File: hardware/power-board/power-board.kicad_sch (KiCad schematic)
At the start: 25 parts, among them J1 SW_SPST, J2 Conn_01x04, J3 DMX512 Out Jack, J4 DMX512, K1 SPST-NO, K2 SPST-NO, P1 IEC320-C14, P2 IEC320-C13, P3 IEC320-C13, U1 NUD3112DMT1G, U2 MAX3075E

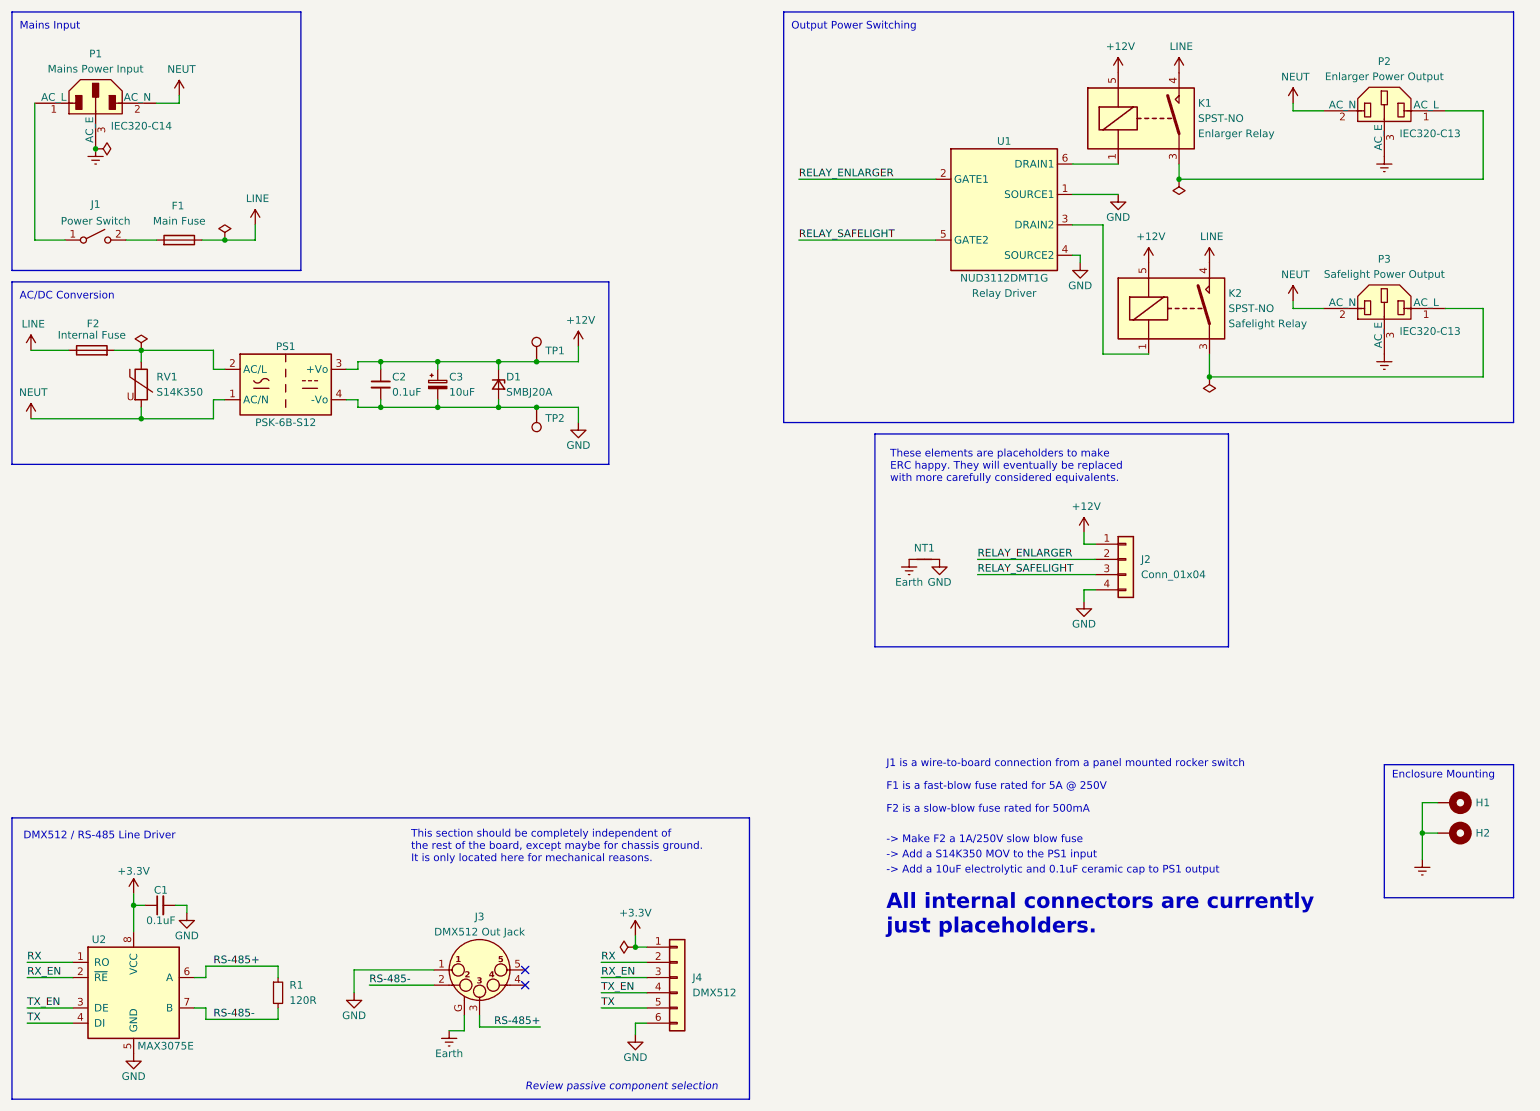
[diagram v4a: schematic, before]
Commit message: Schematic updates and component assignment
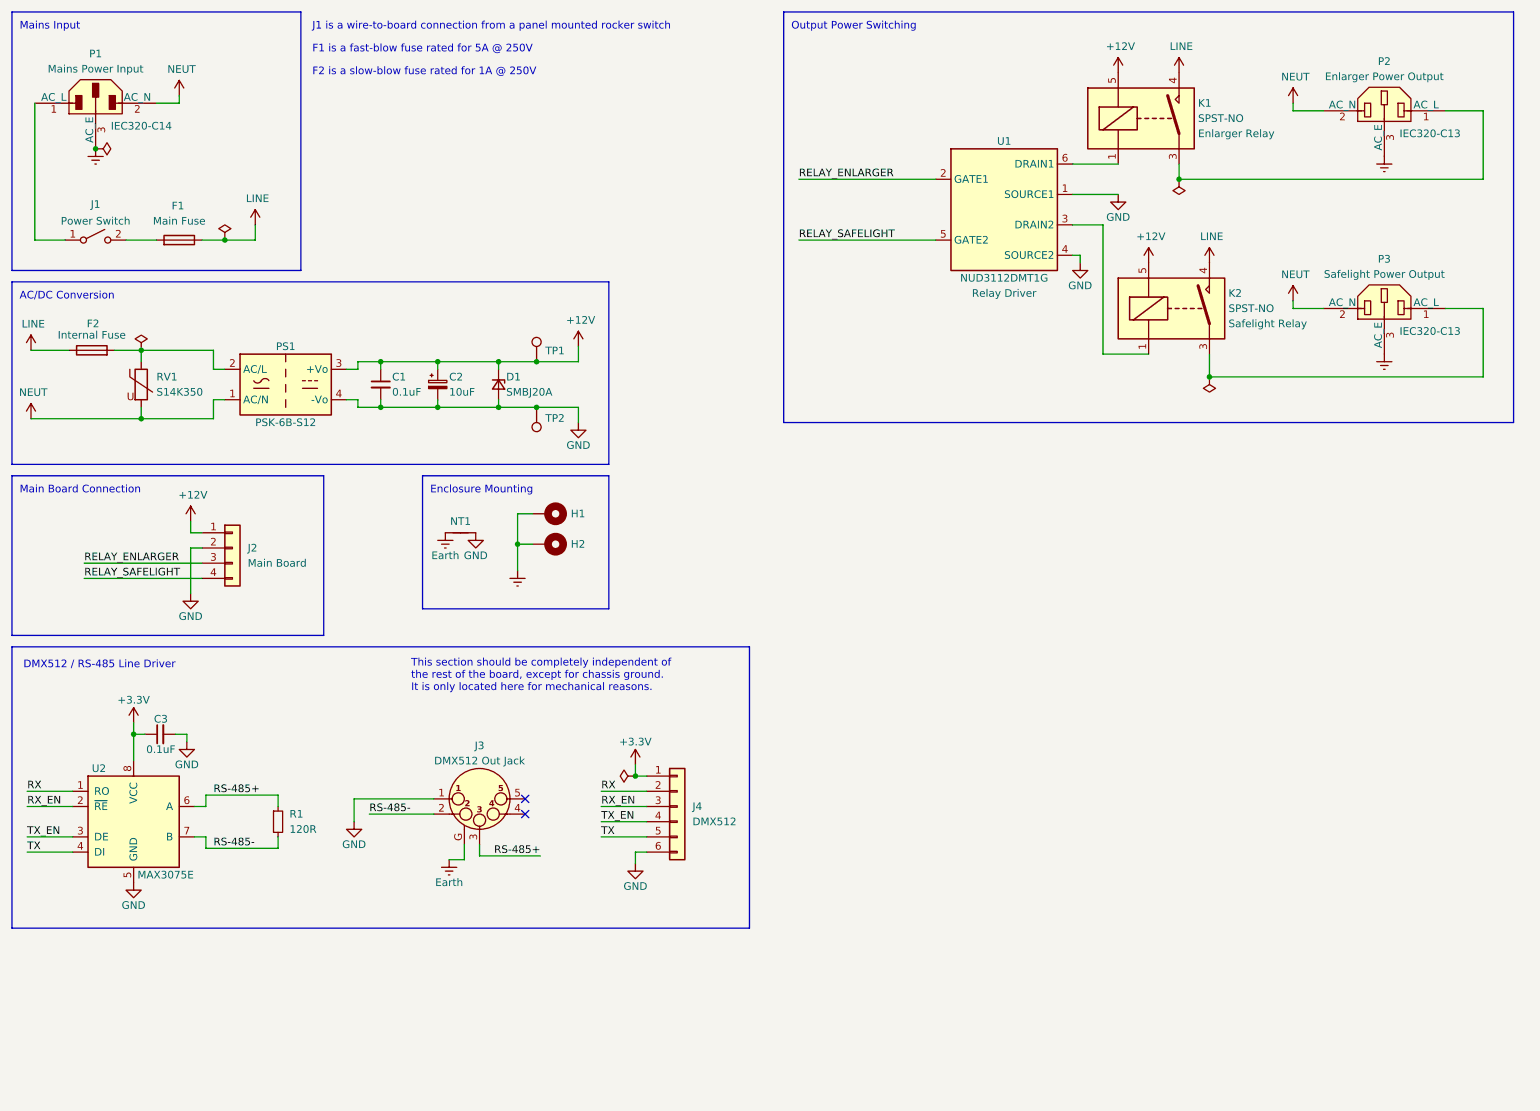
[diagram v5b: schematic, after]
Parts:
- C3: renamed from C1; Manufacturer (none) -> Samsung Electro-Mechanics; Manufacturer PN (none) -> CL21B104KBFNNNE; Supplier (none) -> Digi-Key; Supplier PN (none) -> 1276-1180-1-ND
- J2: value Conn_01x04 -> Main Board; footprint Connector_JST:JST_EH_B4B-EH-A_1x04_P2.50mm_Vertical -> Connector_JST:JST_PH_S4B-PH-SM4-TB_1x04-1MP_P2.00mm_Horizontal; Manufacturer (none) -> JST Sales America Inc.; Manufacturer PN (none) -> S4B-PH-SM4-TB(LF)(SN); Supplier (none) -> Digi-Key; Supplier PN (none) -> 455-1751-1-ND
- J4: footprint Connector_JST:JST_EH_B6B-EH-A_1x06_P2.50mm_Vertical -> Connector_JST:JST_SH_SM06B-SRSS-TB_1x06-1MP_P1.00mm_Horizontal; Manufacturer (none) -> JST Sales America Inc.; Manufacturer PN (none) -> SM06B-SRSS-TB(LF)(SN); Supplier (none) -> Digi-Key; Supplier PN (none) -> 455-1806-1-ND
- R1: Manufacturer (none) -> Vishay Dale; Manufacturer PN (none) -> CRCW0805120RFKEA; Supplier (none) -> Digi-Key; Supplier PN (none) -> 541-120CCT-ND
- renumbered C2 to C1, C3 to C2
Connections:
- net GND: now also J2.2 (Pin_2); no longer J2.4 (Pin_4)
- net RELAY_ENLARGER: now also J2.3 (Pin_3); no longer J2.2 (Pin_2)
- net RELAY_SAFELIGHT: now also J2.4 (Pin_4); no longer J2.3 (Pin_3)
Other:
- note added: "F2 is a slow-blow fuse rated for 1A @ 250V"
- note added: "Main Board Connection"
- note added: "This section should be completely independent of the rest of the board, except for chassis ground. It is only located here for mechanical reasons."
- note removed: "-> Add a 10uF electrolytic and 0.1uF ceramic cap to PS1 output"
- note removed: "-> Add a S14K350 MOV to the PS1 input"
- note removed: "-> Make F2 a 1A/250V slow blow fuse"
- note removed: "All internal connectors are currently just placeholders."
- note removed: "F2 is a slow-blow fuse rated for 500mA"
- note removed: "Review passive component selection"
- note removed: "These elements are placeholders to make ERC happy. They will eventually be replaced with more carefully considered equivalents."
- note removed: "This section should be completely independent of the rest of the board, except maybe for chassis ground. It is only located here for mechanical reasons."
- moved on the sheet: C3, H1, H2, J2, J3, J4, NT1, R1, U2

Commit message: Updated PCB layout, still refining things
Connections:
- net GND: no longer C3.2, J3.1 (P1), J4.6 (Pin_6), U2.5 (GND)
- new net GND1: C3.2, J3.1 (P1), J4.6 (Pin_6), U2.5 (GND)
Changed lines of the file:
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@@
   (junction (at 95.25 80.01) (diameter 0) (color 0 0 0 0)
+  )
+  (junction (at 118.11 154.305) (diameter 0) (color 0 0 0 0)
   )
   (junction (at 49.53 52.07) (diameter 0) (color 0 0 0 0)
@@
     (pin "2")
   )
-  (symbol (lib_id "power:GND") (at 43.18 135.89 0) (unit 1)
-    (in_bom yes) (on_board yes)
-    (property "Reference" "#PWR023" (id 0) (at 43.18 142.24 0)
-      (effects (font (size 1.27 1.27)) hide)
-    )
-    (property "Value" "GND" (id 1) (at 43.18 139.7 0))
-    (property "Footprint" "" (id 2) (at 43.18 135.89 0)
-      (effects (font (size 1.27 1.27)) hide)
-    )
-    (property "Datasheet" "" (id 3) (at 43.18 135.89 0)
-      (effects (font (size 1.27 1.27)) hide)
-    )
-    (pin "1")
-  )
   (symbol (lib_id "Project:Conn_PX0580-PC") (at 27.94 29.21 0) (unit 1)
     (in_bom yes) (on_board yes)
@@
     (pin "2")
     (pin "3")
+  )
+  (symbol (lib_id "power:GND1") (at 118.11 156.21 0) (unit 1)
+    (in_bom yes) (on_board yes)
+    (property "Reference" "#PWR028" (id 0) (at 118.11 162.56 0)
+      (effects (font (size 1.27 1.27)) hide)
+    )
+    (property "Value" "GND1" (id 1) (at 118.11 160.02 0))
+    (property "Footprint" "" (id 2) (at 118.11 156.21 0)
+      (effects (font (size 1.27 1.27)) hide)
+    )
+    (property "Datasheet" "" (id 3) (at 118.11 156.21 0)
+      (effects (font (size 1.27 1.27)) hide)
+    )
+    (pin "1")
+  )
+  (symbol (lib_id "power:GND1") (at 43.18 135.89 0) (unit 1)
+    (in_bom yes) (on_board yes)
+    (property "Reference" "#PWR023" (id 0) (at 43.18 142.24 0)
+      (effects (font (size 1.27 1.27)) hide)
+    )
+    (property "Value" "GND1" (id 1) (at 43.18 139.7 0))
+    (property "Footprint" "" (id 2) (at 43.18 135.89 0)
+      (effects (font (size 1.27 1.27)) hide)
+    )
+    (property "Datasheet" "" (id 3) (at 43.18 135.89 0)
+      (effects (font (size 1.27 1.27)) hide)
+    )
+    (pin "1")
   )
   (symbol (lib_id "Device:NetTie_2") (at 88.9 100.965 0) (unit 1)
@@
     (pin "1")
     (pin "2")
+  )
+  (symbol (lib_id "power:GND1") (at 34.29 159.385 0) (unit 1)
+    (in_bom yes) (on_board yes)
+    (property "Reference" "#PWR022" (id 0) (at 34.29 165.735 0)
+      (effects (font (size 1.27 1.27)) hide)
+    )
+    (property "Value" "GND1" (id 1) (at 34.29 163.195 0))
+    (property "Footprint" "" (id 2) (at 34.29 159.385 0)
+      (effects (font (size 1.27 1.27)) hide)
+    )
+    (property "Datasheet" "" (id 3) (at 34.29 159.385 0)
+      (effects (font (size 1.27 1.27)) hide)
+    )
+    (pin "1")
   )
   (symbol (lib_id "power:+12V") (at 198.755 24.13 0) (unit 1)
@@
     (pin "1")
   )
-  (symbol (lib_id "power:GND") (at 118.11 156.21 0) (unit 1)
-    (in_bom yes) (on_board yes)
-    (property "Reference" "#PWR028" (id 0) (at 118.11 162.56 0)
-      (effects (font (size 1.27 1.27)) hide)
-    )
-    (property "Value" "GND" (id 1) (at 118.11 160.02 0))
-    (property "Footprint" "" (id 2) (at 118.11 156.21 0)
-      (effects (font (size 1.27 1.27)) hide)
-    )
-    (property "Datasheet" "" (id 3) (at 118.11 156.21 0)
-      (effects (font (size 1.27 1.27)) hide)
-    )
-    (pin "1")
-  )
   (symbol (lib_id "Device:C_Small") (at 38.735 134.62 90) (unit 1)
     (in_bom yes) (on_board yes)
@@
     )
     (property "Datasheet" "~" (id 3) (at 243.205 71.12 0)
+      (effects (font (size 1.27 1.27)) hide)
+    )
+    (pin "1")
+  )
+  (symbol (lib_id "power:PWR_FLAG") (at 118.11 154.305 90) (unit 1)
+    (in_bom yes) (on_board yes)
+    (property "Reference" "#FLG07" (id 0) (at 116.205 154.305 0)
+      (effects (font (size 1.27 1.27)) hide)
+    )
+    (property "Value" "PWR_FLAG" (id 1) (at 114.3 154.305 0)
+      (effects (font (size 1.27 1.27)) hide)
+    )
+    (property "Footprint" "" (id 2) (at 118.11 154.305 0)
+      (effects (font (size 1.27 1.27)) hide)
+    )
+    (property "Datasheet" "~" (id 3) (at 118.11 154.305 0)
       (effects (font (size 1.27 1.27)) hide)
     )
@@
     (pin "1")
   )
-  (symbol (lib_id "power:GND") (at 71.12 149.225 0) (unit 1)
-    (in_bom yes) (on_board yes)
-    (property "Reference" "#PWR024" (id 0) (at 71.12 155.575 0)
-      (effects (font (size 1.27 1.27)) hide)
-    )
-    (property "Value" "GND" (id 1) (at 71.12 153.035 0))
-    (property "Footprint" "" (id 2) (at 71.12 149.225 0)
-      (effects (font (size 1.27 1.27)) hide)
-    )
-    (property "Datasheet" "" (id 3) (at 71.12 149.225 0)
-      (effects (font (size 1.27 1.27)) hide)
-    )
-    (pin "1")
-  )
   (symbol (lib_id "power:PWR_FLAG") (at 27.94 36.83 270) (unit 1)
     (in_bom yes) (on_board yes)
@@
     (pin "1")
   )
-  (symbol (lib_id "power:GND") (at 34.29 159.385 0) (unit 1)
-    (in_bom yes) (on_board yes)
-    (property "Reference" "#PWR022" (id 0) (at 34.29 165.735 0)
-      (effects (font (size 1.27 1.27)) hide)
-    )
-    (property "Value" "GND" (id 1) (at 34.29 163.195 0))
-    (property "Footprint" "" (id 2) (at 34.29 159.385 0)
-      (effects (font (size 1.27 1.27)) hide)
-    )
-    (property "Datasheet" "" (id 3) (at 34.29 159.385 0)
-      (effects (font (size 1.27 1.27)) hide)
-    )
-    (pin "1")
-  )
   (symbol (lib_id "Project:PSK-6B-S12") (at 59.69 76.2 0) (unit 1)
     (in_bom yes) (on_board yes)
@@
     )
     (property "Datasheet" "" (id 3) (at 208.915 24.13 0)
+      (effects (font (size 1.27 1.27)) hide)
+    )
+    (pin "1")
+  )
+  (symbol (lib_id "power:GND1") (at 71.12 149.225 0) (unit 1)
+    (in_bom yes) (on_board yes)
+    (property "Reference" "#PWR024" (id 0) (at 71.12 155.575 0)
+      (effects (font (size 1.27 1.27)) hide)
+    )
+    (property "Value" "GND1" (id 1) (at 71.12 153.035 0))
+    (property "Footprint" "" (id 2) (at 71.12 149.225 0)
+      (effects (font (size 1.27 1.27)) hide)
+    )
+    (property "Datasheet" "" (id 3) (at 71.12 149.225 0)
       (effects (font (size 1.27 1.27)) hide)
     )
@@
       (reference "#FLG06") (unit 1) (value "PWR_FLAG") (footprint "")
     )
+    (path "/ad7505eb-addd-47cc-b830-1245109c476f"
+      (reference "#FLG07") (unit 1) (value "PWR_FLAG") (footprint "")
+    )
     (path "/f3f865b6-c7a0-4dde-9cf7-4763a1295ea1"
       (reference "#PWR01") (unit 1) (value "Earth") (footprint "")
@@
       (reference "#PWR021") (unit 1) (value "GND") (footprint "")
     )
-    (path "/f414fade-2297-4152-a754-c86f8c9e7f90"
-      (reference "#PWR022") (unit 1) (value "GND") (footprint "")
-    )
-    (path "/203ef615-4332-432b-b07c-2f82589530ea"
-      (reference "#PWR023") (unit 1) (value "GND") (footprint "")
-    )
-    (path "/e8afdcb2-93ca-4bac-b467-43551ac02a9b"
-      (reference "#PWR024") (unit 1) (value "GND") (footprint "")
+    (path "/53d9ccd4-509a-405c-b060-9272127d6e5b"
+      (reference "#PWR022") (unit 1) (value "GND1") (footprint "")
+    )
+    (path "/3b543809-26ac-49f8-a798-fec846360a65"
+      (reference "#PWR023") (unit 1) (value "GND1") (footprint "")
+    )
+    (path "/f6ff6ac4-3ace-4502-84b0-e74ef7bc8c30"
+      (reference "#PWR024") (unit 1) (value "GND1") (footprint "")
     )
     (path "/09bf7df5-a2b0-47eb-a4b1-0b40fec050f0"
@@
       (reference "#PWR027") (unit 1) (value "+3.3V") (footprint "")
     )
-    (path "/8175dd0f-f2fb-4914-bbe2-cee03a8b3fe4"
-      (reference "#PWR028") (unit 1) (value "GND") (footprint "")
+    (path "/2845f656-79ca-460c-83c1-44f85268f74d"
+      (reference "#PWR028") (unit 1) (value "GND1") (footprint "")
     )
     (path "/9ede84d3-7953-48bb-a396-f023a59e5ad5"

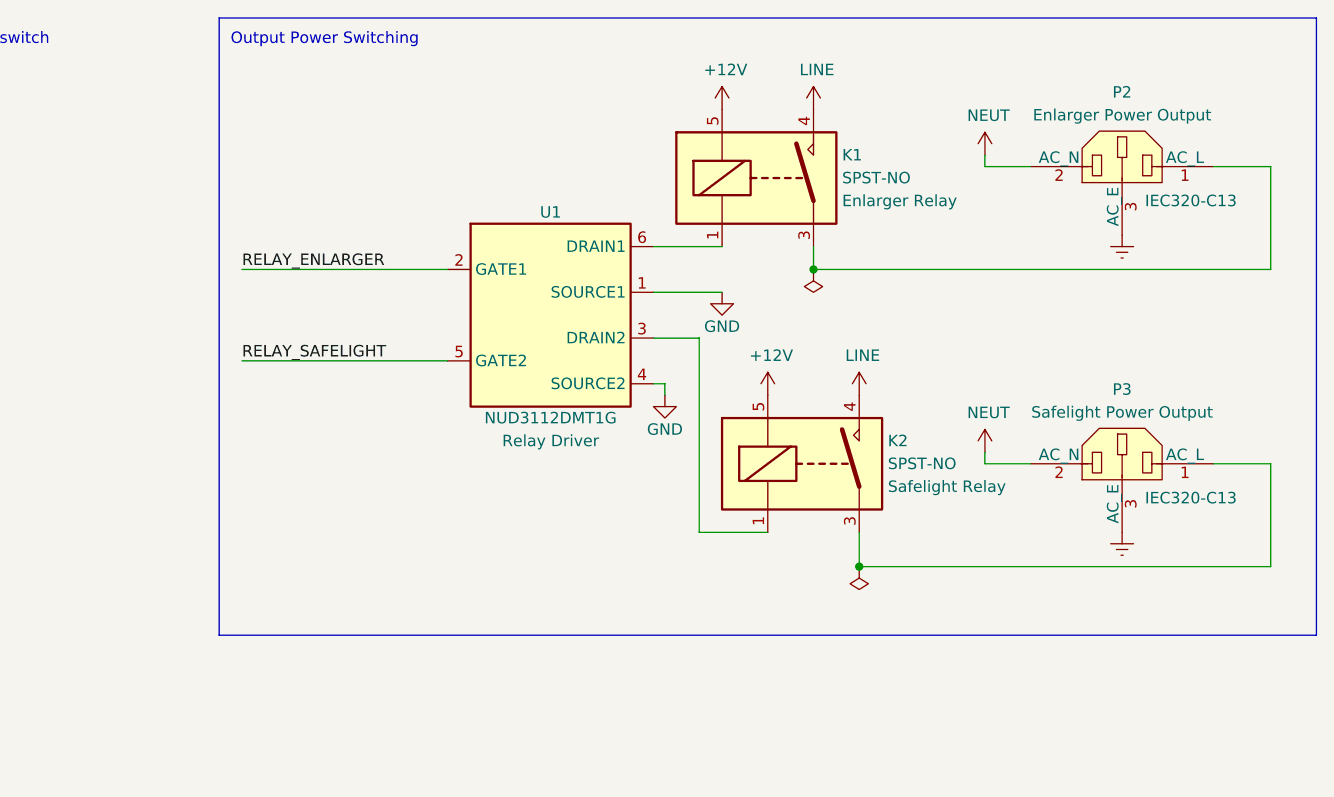
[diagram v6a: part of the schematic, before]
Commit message: Symbol and PCB layout tweaks
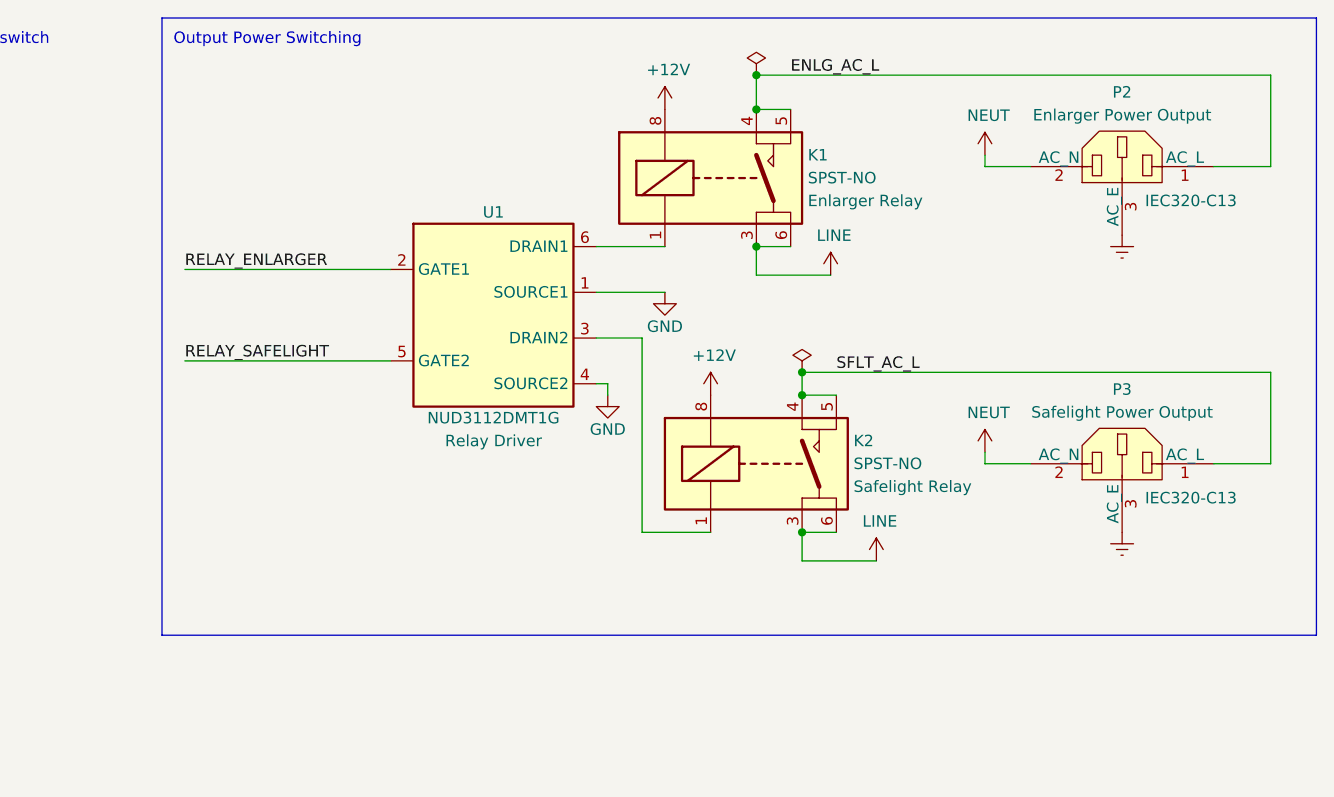
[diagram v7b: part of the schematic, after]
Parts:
- K1, K2: footprint lib_fp:Relay_SPST_Omron_G2RL-1A -> lib_fp:Relay_SPST_Omron_G2RL-1A-E; symbol Project:G2RL-1A4-DC12 -> Project:G2RL-1A4-E-DC12; Manufacturer PN G2RL-1A4 DC12 -> G2RL-1A4-E DC12; Supplier PN Z2923-ND -> Z3083-ND
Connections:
- net +12V: now also K1.8, K2.8; no longer K1.5, K2.5
- net LINE: now also K1.3, K1.6, K2.3, K2.6; no longer K1.4, K2.4
- net SFLT_AC_L: now reaches P3.1 (AC_L)
- net SFLT_AC_L: now also K2.4, K2.5; no longer K2.3
- net ENLG_AC_L: now reaches P2.1 (AC_L)
- net ENLG_AC_L: now also K1.4, K1.5; no longer K1.3
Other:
- moved on the sheet: U1
